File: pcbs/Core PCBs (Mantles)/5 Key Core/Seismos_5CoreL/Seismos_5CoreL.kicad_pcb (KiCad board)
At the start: 2 copper layers, 147 x 78 mm, 27 parts, among them J1 SM09B-SRSS-TB(LF)(SN), J2 SM09B-SRSS-TB(LF)(SN), J3 SM09B-SRSS-TB(LF)(SN), J4 SM09B-SRSS-TB(LF)(SN), J5 SM09B-SRSS-TB(LF)(SN), J6 SM09B-SRSS-TB(LF)(SN), J7 SM09B-SRSS-TB(LF)(SN), J8 MJ-4PP-9-Lily58, J9 Conn_01x05_Pin, SW1 RotaryEncoder_Switch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

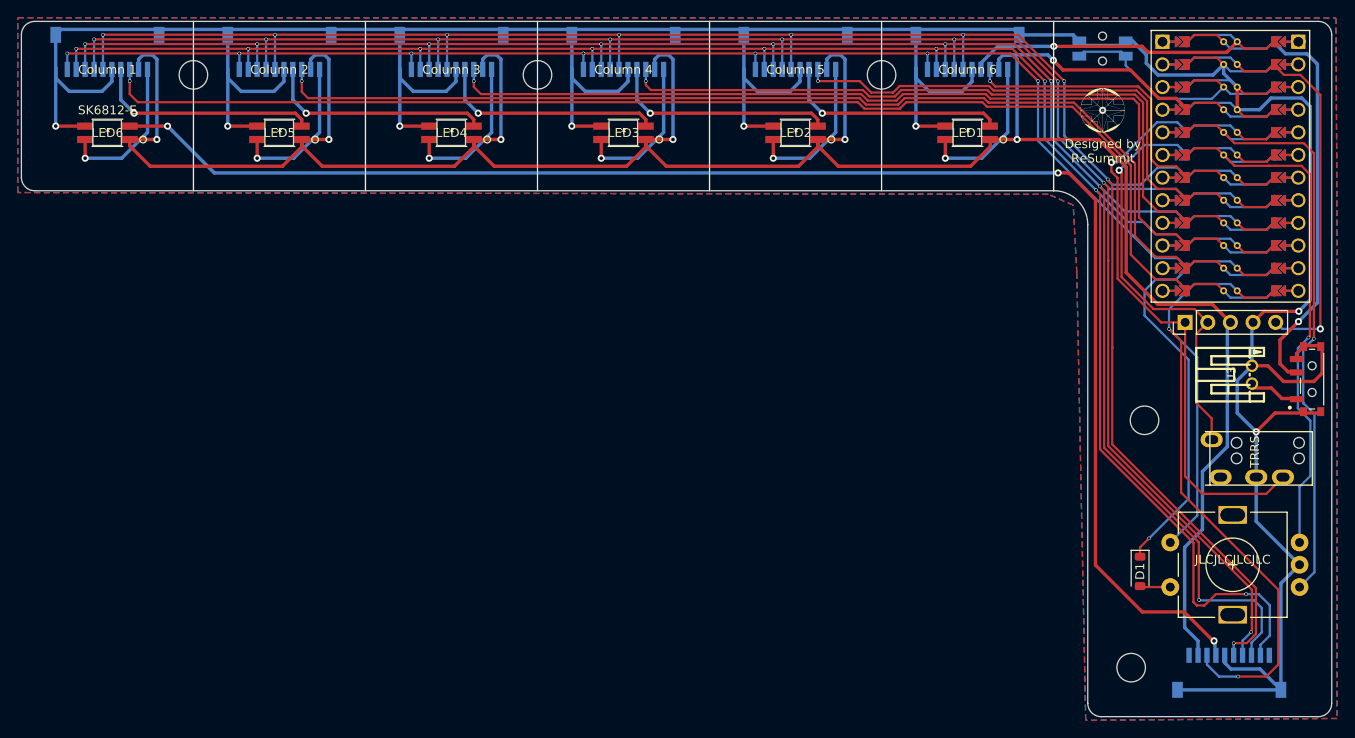
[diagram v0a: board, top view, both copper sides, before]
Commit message: Release v1.1
***NOTE***: If you have a previous commit, please update your files.
This commit fixes the incorrect RGB pinout and power switch as the
RGB footprint was incorrect.
The power switch behaviour is also fixed in this commit so the position
matches on both sides.
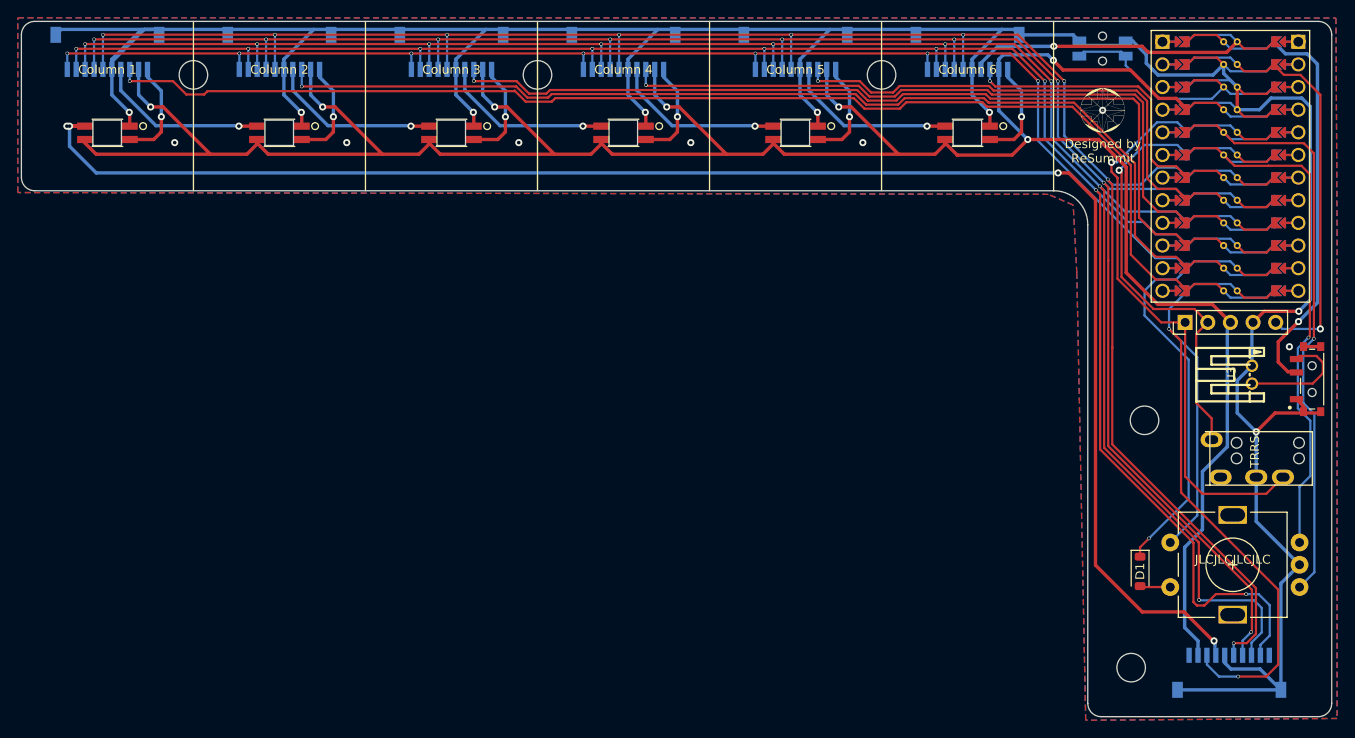
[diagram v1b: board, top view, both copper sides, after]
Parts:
- LED1, LED2, LED3, LED4, LED5, LED6: moved to F.Cu
- turned LED1 to 180 degrees
- turned LED2 to 180 degrees
- turned LED3 to 180 degrees
- turned LED4 to 180 degrees
- turned LED5 to 180 degrees
- turned LED6 to 180 degrees
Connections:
- U2 pad L1: GND -> Net-(U2-PadL1)
- U2 pad L2: Net-(U2-PadL2) -> GND
- U3 pad 2: Net-(U2-PadL2) -> Net-(U2-PadL1)
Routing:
- net GND: track 406.3 -> 341.8 mm, vias 9 -> 15
- net Net-(U2-PadL1): track 0.00 -> 13.1 mm
- net /V+: track 309.8 -> 297.8 mm
- net /RGB_In7: track 170.2 -> 182.1 mm, vias 3 -> 4
- net /RGB_In5: track 25.4 -> 19.3 mm
- net /RGB_In6: track 25.4 -> 19.3 mm
- net /RGB_In2: track 25.4 -> 19.3 mm
- net /RGB_In4: track 25.4 -> 19.3 mm
- net /RGB_In3: track 25.4 -> 19.3 mm
- net /RGB_Out1: track 17.3 -> 11.6 mm
- net /RGB_Out4: track 17.3 -> 11.6 mm
- net /RGB_Out5: track 17.3 -> 11.6 mm
- net /RGB_Out3: track 17.3 -> 11.6 mm
- net /RGB_Out6: track 17.3 -> 11.6 mm
- net /RGB_Out2: track 17.3 -> 11.6 mm
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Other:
- board text added: "Rev. 1.1"
- board text removed: "Rev. 1.0"

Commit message: Release v1.1.1
Added I2C pull up resistors and bridge contacts on the backif 5V power
is desired. If you have v1.1, V+ is actually close to the headphone
jack, so you can scratch off the trace and bridge there.
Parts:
- added JP1: Jumper_2_Open, Jumper:SolderJumper-2_P1.3mm_Open_TrianglePad1.0x1.5mm, B.Cu at (162.9, 71.2)
- added R1: R, Resistor_SMD:R_0603_1608Metric_Pad0.98x0.95mm_HandSolder, B.Cu at (166.3, 63.7)
- added R2: R, Resistor_SMD:R_0603_1608Metric_Pad0.98x0.95mm_HandSolder, B.Cu at (164.3, 63.7)
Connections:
- J8 pad 1: unconnected-(J8-Pad1) -> Net-(JP1-A)
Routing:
- net GND: track 341.8 -> 307.7 mm, vias 15 -> 14
- net SDA: track 63.6 -> 73.7 mm
- net SCL: track 47.6 -> 50.2 mm
- net /V+: track 297.8 -> 299.8 mm
- net /Col_InT: track 84.5 -> 83.5 mm
- net /Row5: track 190.3 -> 189.7 mm
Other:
- board text added: "Rev. 1.1.1"
- board text removed: "Rev. 1.1"

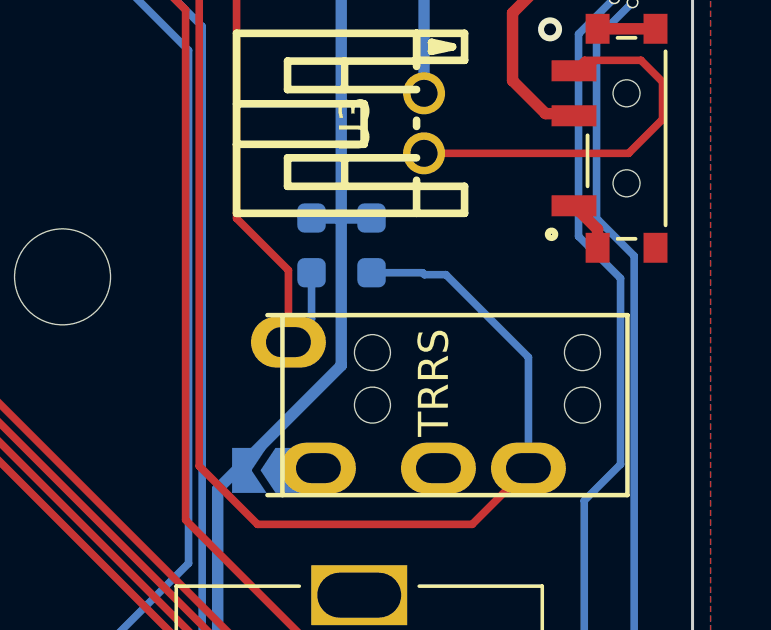
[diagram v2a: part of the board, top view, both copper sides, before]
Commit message: Fix right encoder button, fix connector refs
Right side encoder was still connected to the 6th column for some
reason... Figures when you copy paste the same board design into a
different project.

Also fixed references for the SH connectors, so it doesn't look weird
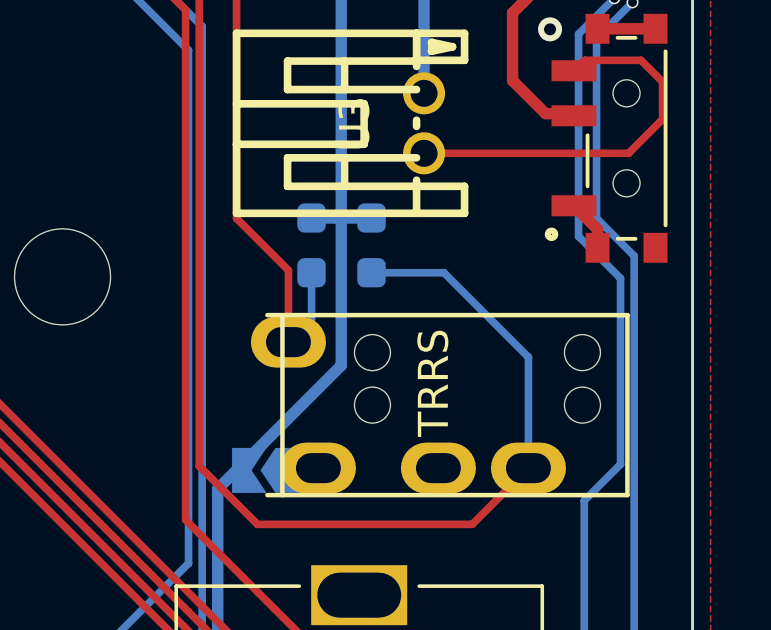
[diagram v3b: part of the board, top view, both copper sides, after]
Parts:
- J1, J2, J3, J4, J5, J6: value SM09B-SRSS-TB(LF)(SN) -> SM010B-SRSS-TB(LF)(SN)
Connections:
- SW1 pad MP: (no net) -> GND
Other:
- board text added: "Rev. 1.1.2"
- board text removed: "Rev. 1.1.1"

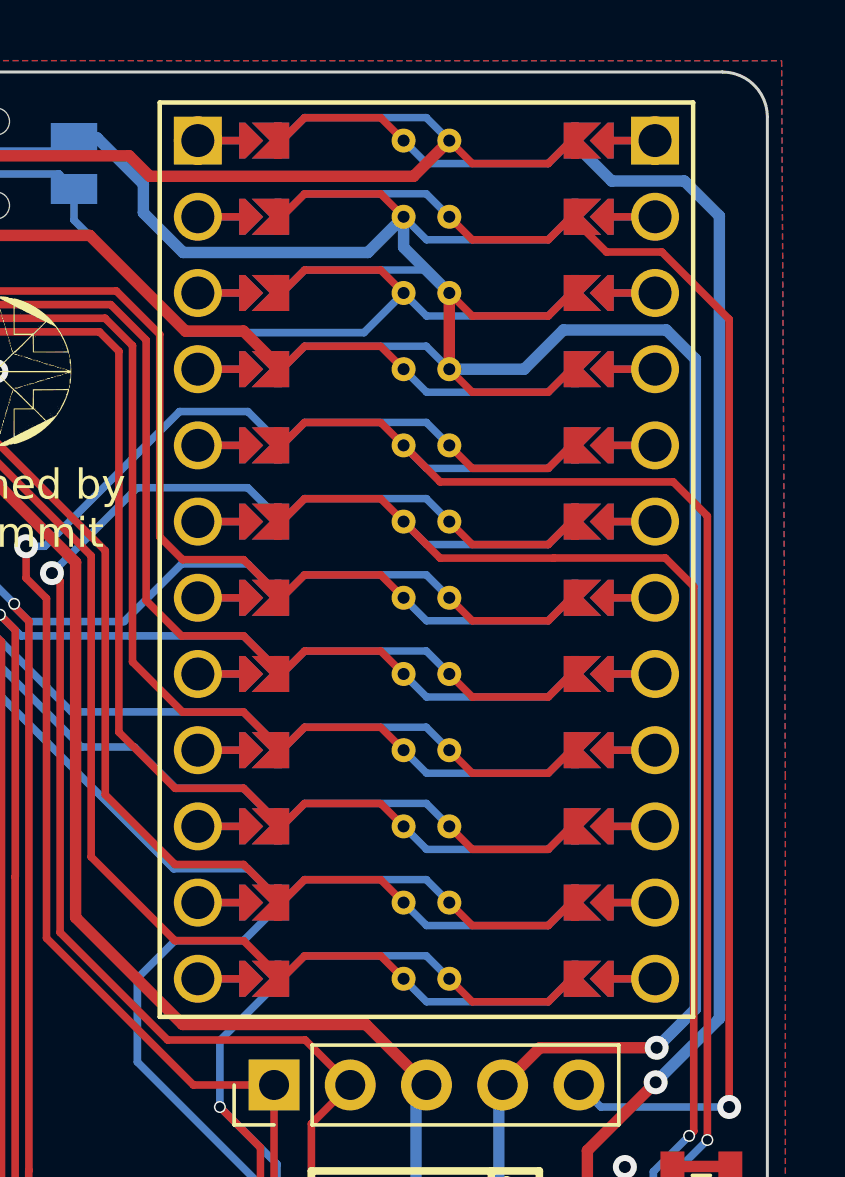
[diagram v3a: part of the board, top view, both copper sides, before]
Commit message: Added 74HC595A support, new release
New PCB versions supporting shift register.
Another JST SH connector is added to expose 2 spare pins.

Footprints for microcontroller were updated using modified footprint from library.
Original variants updated to these new footprints with some fixes as well.
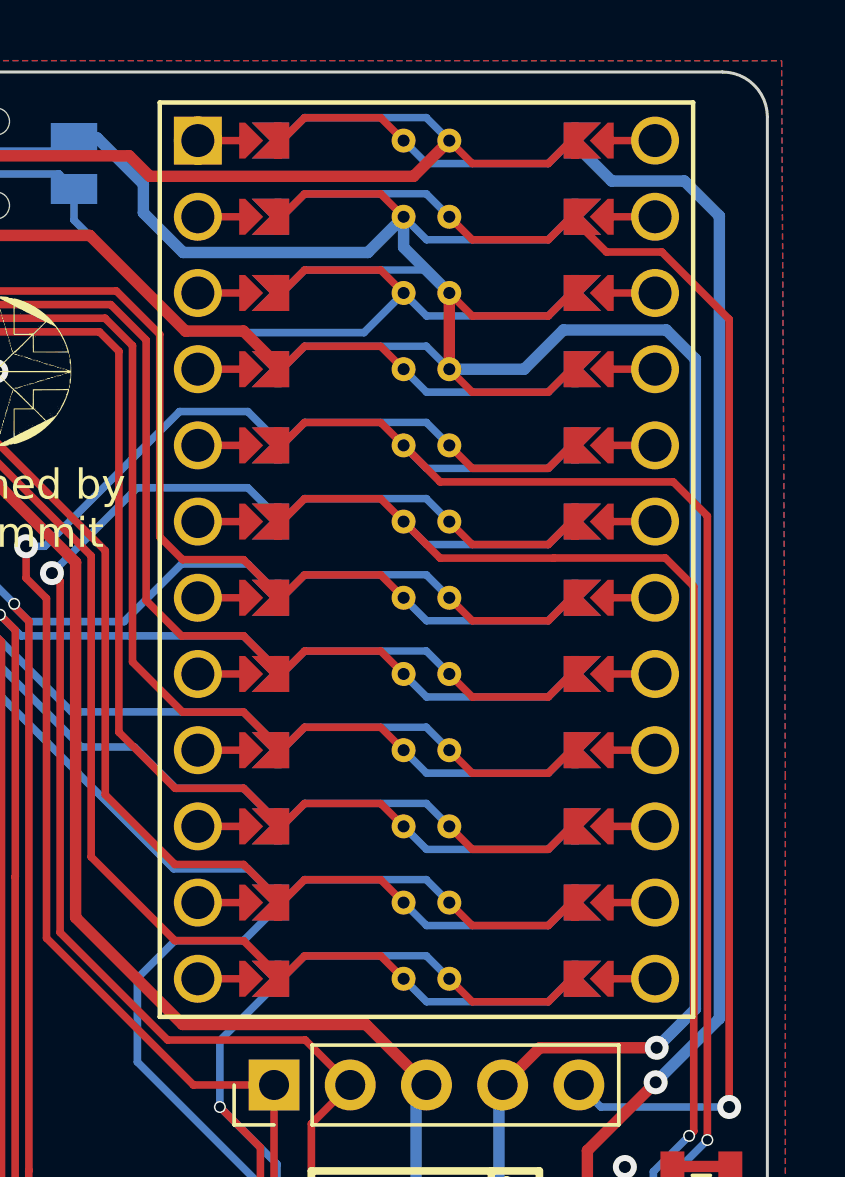
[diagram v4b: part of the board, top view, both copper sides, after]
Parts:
- J7: value SM09B-SRSS-TB(LF)(SN) -> SM10B-SRSS-TB_(LF)(SN)
- U1: footprint keyboard_reversible:ProMicro -> Seismos-libs:keebRev-onesided_ProMicro
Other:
- board text added: "Rev. 2.0.0"
- board text removed: "Rev. 1.1.2"

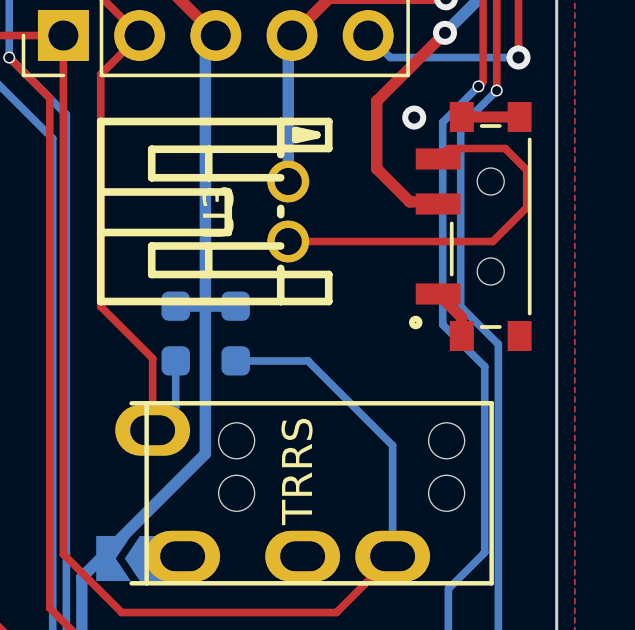
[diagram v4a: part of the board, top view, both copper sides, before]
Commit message: HOTFIX, power switch bridges to ground
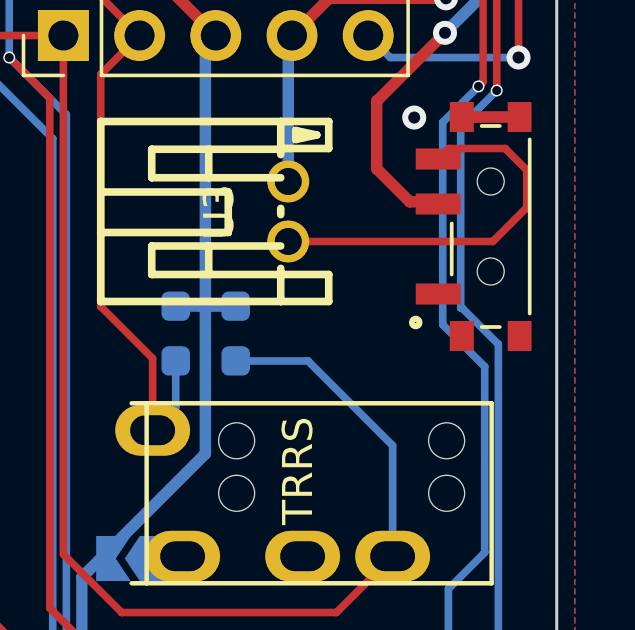
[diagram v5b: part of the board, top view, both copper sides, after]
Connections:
- U2 pad L2: GND -> unconnected-(U2-PadL2)
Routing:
- net GND: track 307.7 -> 305.9 mm

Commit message: Update PCB version and gerbers for HOTFIX
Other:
- board text added: "Rev. 2.1.0"
- board text removed: "Rev. 2.0.0"
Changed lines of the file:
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@@
 		(layer "Edge.Cuts")
 	)
-	(gr_text "Rev. 2.0.0"
+	(gr_text "Rev. 2.1.0"
 		(at 153.55 78.9 270)
 		(layer "B.SilkS")
